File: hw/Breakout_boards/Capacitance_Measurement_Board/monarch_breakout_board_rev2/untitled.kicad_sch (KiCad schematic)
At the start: 11 parts, among them J1 2200980471, J2 2200980471, J3 2200980471

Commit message: Breakout Boards Measurements
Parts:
- added J4: 2200980471, Connector_Molex_Micro-Lock-Plus:Molex_Micro-Lock_2200980471_1x04_P1.25mm_Horizontal, symbol 5037630491:5037630491
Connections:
- net +3V3: now also J4.4
- net GND: now also J4.3
- net I2C4_SCL: now also J4.1
- net I2C4_SDA: now also J4.2
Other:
- note added: "Breakout Board Connection"

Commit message: New REV2 Breakout Board Schematic Done
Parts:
- removed J1, J2, J4: 2200980471, Connector_Molex_Micro-Lock-Plus:Molex_Micro-Lock_2200980471_1x04_P1.25mm_Horizontal, symbol 5037630491:5037630491
- added J11, J12, J13, J14, J5, J7, J8, J9: Conn_Coaxial, symbol Connector:Conn_Coaxial
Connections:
- net Cap0+: now also J5.1 (In)
- net Cap0-: now also J7.1 (In)
- net Cap1+: now also J8.1 (In)
- net Cap1-: now also J9.1 (In)
- net Cap2+: now also J11.1 (In)
- net Cap2-: now also J12.1 (In)
- net Cap3+: now also J13.1 (In)
- net Cap3-: now also J14.1 (In)
- net GND: now also J11.2 (Ext), J12.2 (Ext), J13.2 (Ext), J14.2 (Ext), J5.2 (Ext), J7.2 (Ext), J8.2 (Ext), J9.2 (Ext)
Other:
- note removed: "Breakout Board Connection"
- company: (none) -> EP + LASSI LAB
- title: (none) -> Breakout Board
- moved on the sheet: H1, H2, H3, H4, J3, TP1, TP2, TP3, TP4

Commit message: Capacitance Board Schematic Done - Ran into issue with too big of BNC connectors
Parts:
- removed J11, J12, J13, J14, J9: Conn_Coaxial, symbol Connector:Conn_Coaxial
- added J2, J3, J4, J5, J6: Conn_Coaxial, BNC_Adam_Tech:RF101AD0075M, symbol Connector:Conn_Coaxial
- J1: renamed from J5; footprint (none) -> BNC_Adam_Tech:RF101AD0075M
- J7, J8: footprint (none) -> BNC_Adam_Tech:RF101AD0075M
- renumbered J3 to J9
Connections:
- net Cap0-: now also J2.1 (In); no longer J7.1 (In)
- net Cap1+: now also J3.1 (In); no longer J8.1 (In)
- net Cap1-: now also J4.1 (In)
- net Cap2+: now also J5.1 (In)
- net Cap2-: now also J6.1 (In)
- net Cap3+: now also J7.1 (In)
- net Cap3-: now also J8.1 (In)
- net GND: now also J2.2 (Ext), J3.2 (Ext), J4.2 (Ext), J5.2 (Ext), J6.2 (Ext)

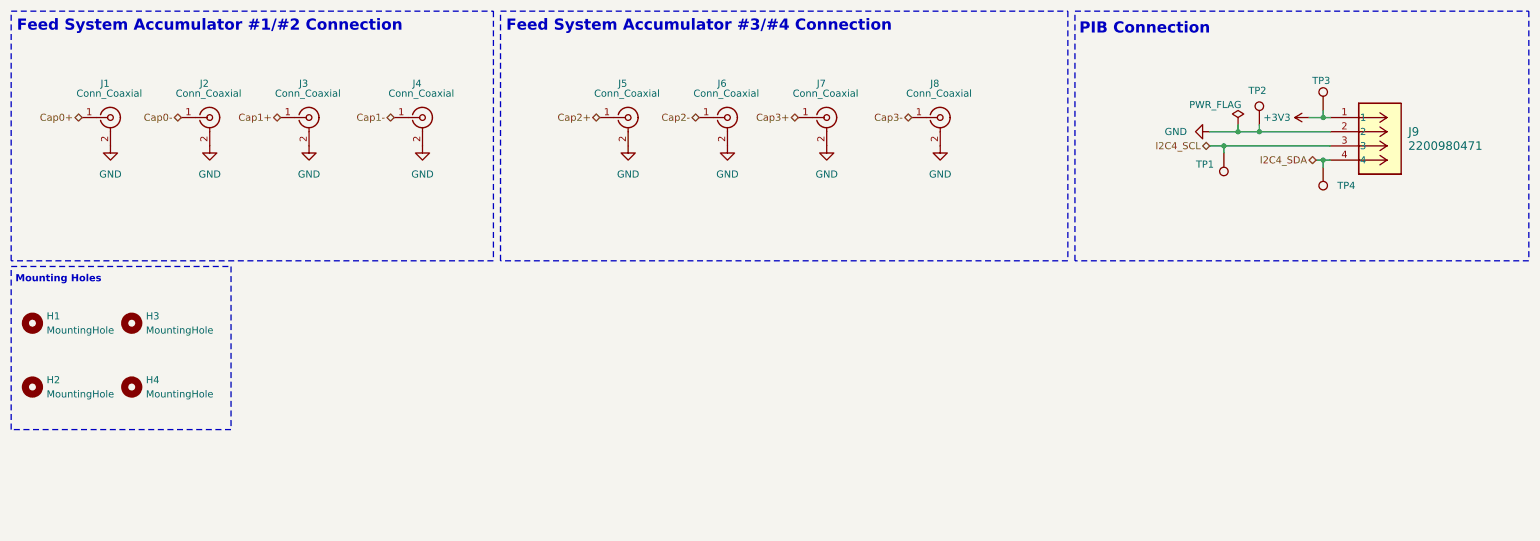
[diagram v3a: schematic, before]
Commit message: Close Valve Cmds implementation + AD7124 + port over correct drivers
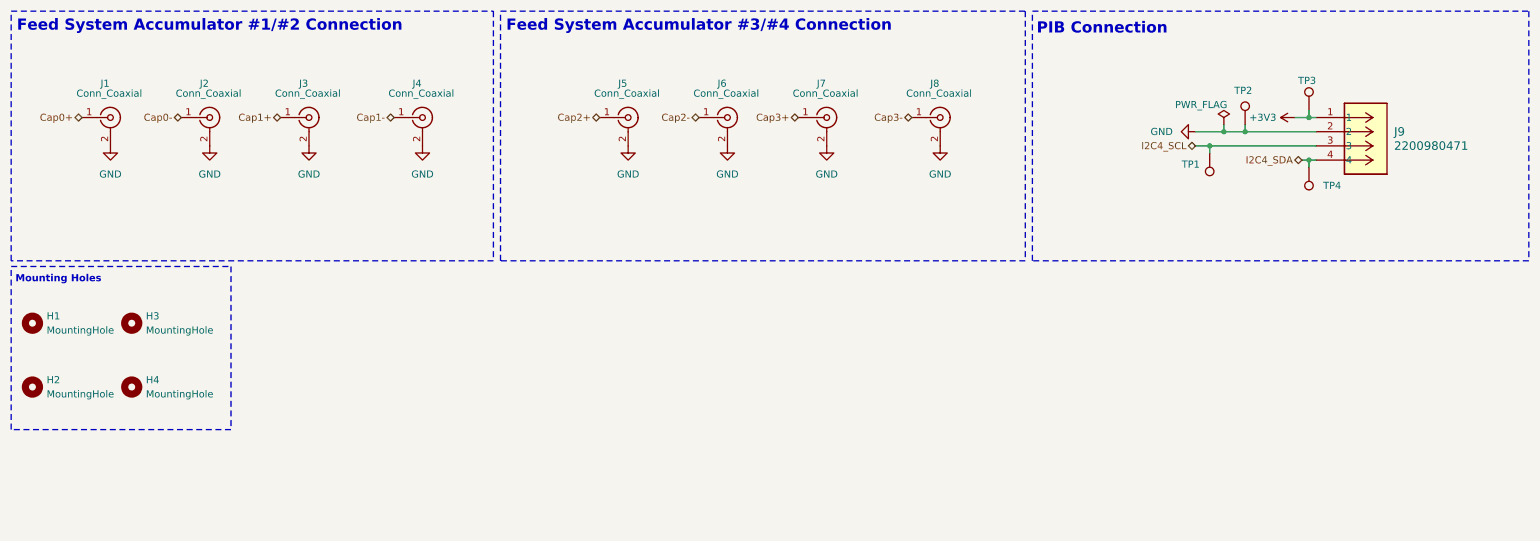
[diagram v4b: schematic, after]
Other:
- title: Breakout Board -> Capacitance Measurement Board
- moved on the sheet: J9, TP1, TP2, TP3, TP4

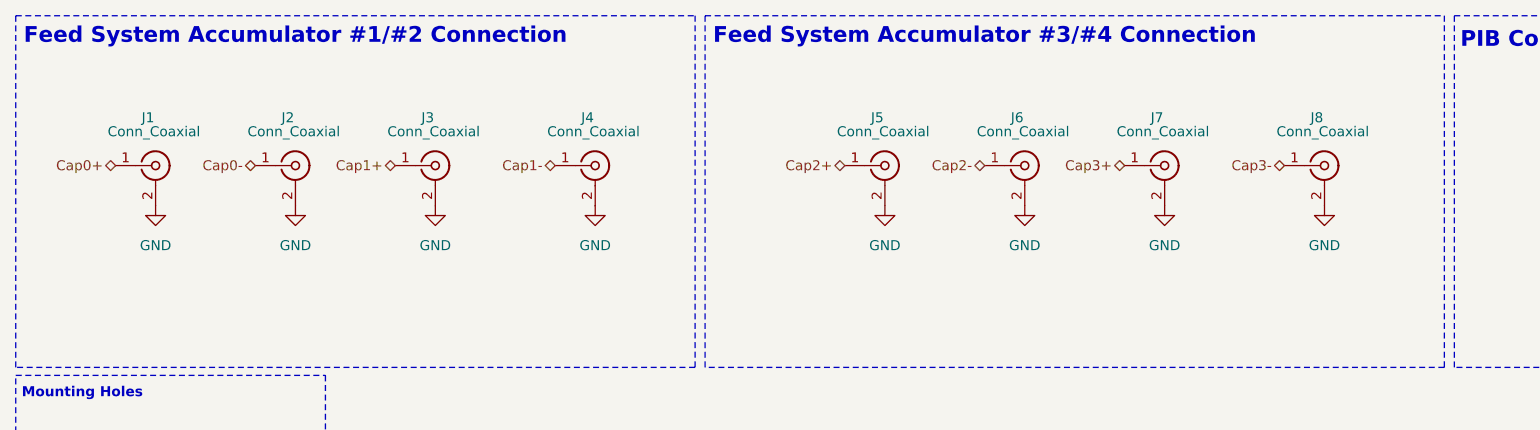
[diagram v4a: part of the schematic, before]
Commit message: Added Micro-Lock Connectors
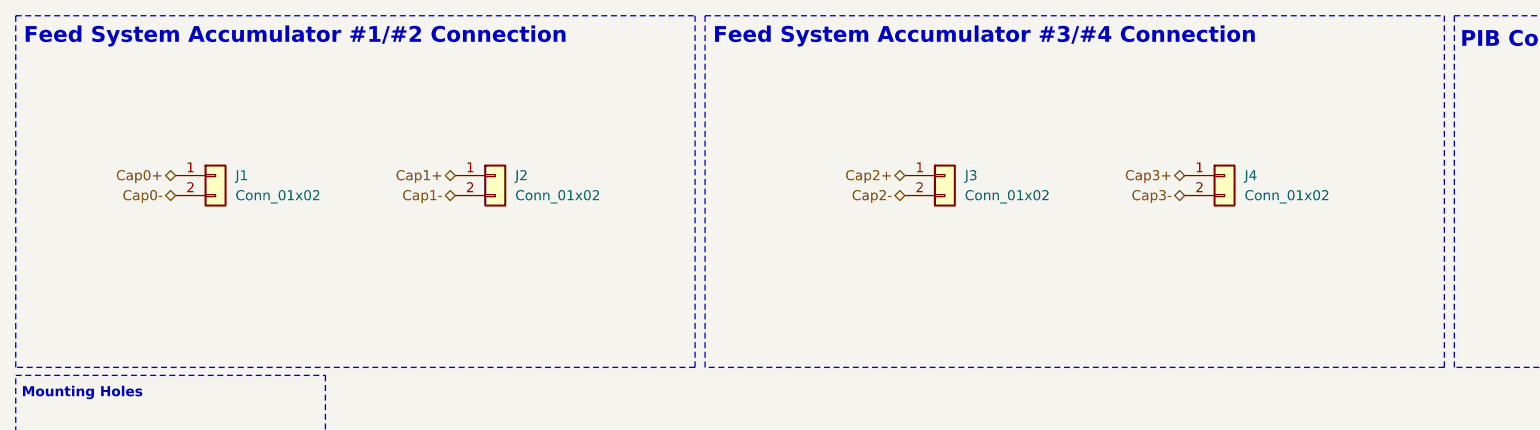
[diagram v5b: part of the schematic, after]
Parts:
- removed J1, J2, J3, J4, J5, J6, J7, J8: Conn_Coaxial, BNC_Adam_Tech:RF101AD0075M, symbol Connector:Conn_Coaxial
- added J1, J2, J3, J4: Conn_01x02, Connector_Molex_Micro-Lock-Plus:Molex_Micro-Lock_2200980271_1x02_P1.25mm_Horizontal, symbol Connector_Generic:Conn_01x02
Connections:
- net Cap0+: now also J1.1 (Pin_1)
- net Cap0-: now also J1.2 (Pin_2)
- net Cap1+: now also J2.1 (Pin_1)
- net Cap1-: now also J2.2 (Pin_2)
- net Cap2+: now also J3.1 (Pin_1)
- net Cap2-: now also J3.2 (Pin_2)
- net Cap3+: now also J4.1 (Pin_1)
- net Cap3-: now also J4.2 (Pin_2)
